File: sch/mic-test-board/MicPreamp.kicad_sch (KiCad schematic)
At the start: 30 parts, among them U7 ADA4940-2

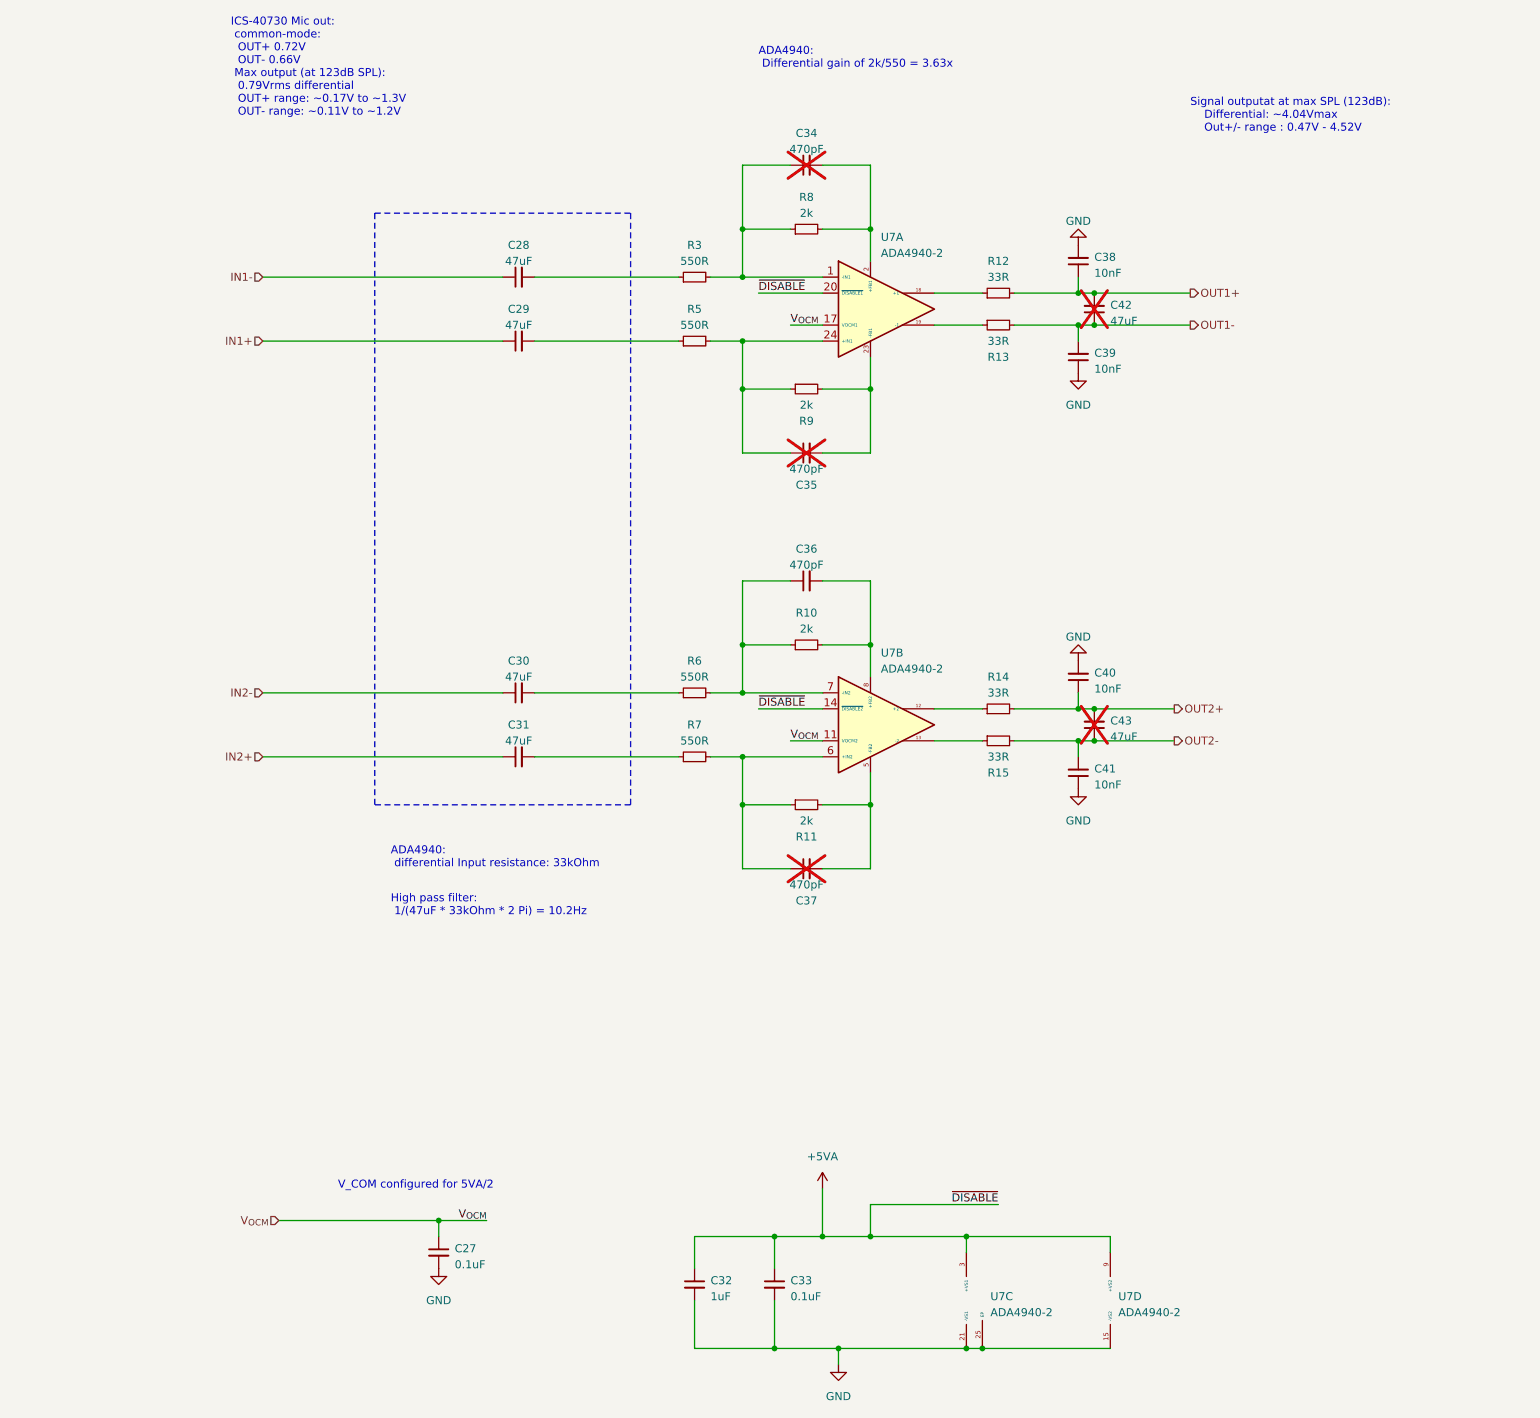
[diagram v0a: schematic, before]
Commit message: pcb: commit before large routing effort
 - schematic refactor to split preamps to each mic board
 - Mic board and main board are placed
 - no tracks laid
 - critical parts selected
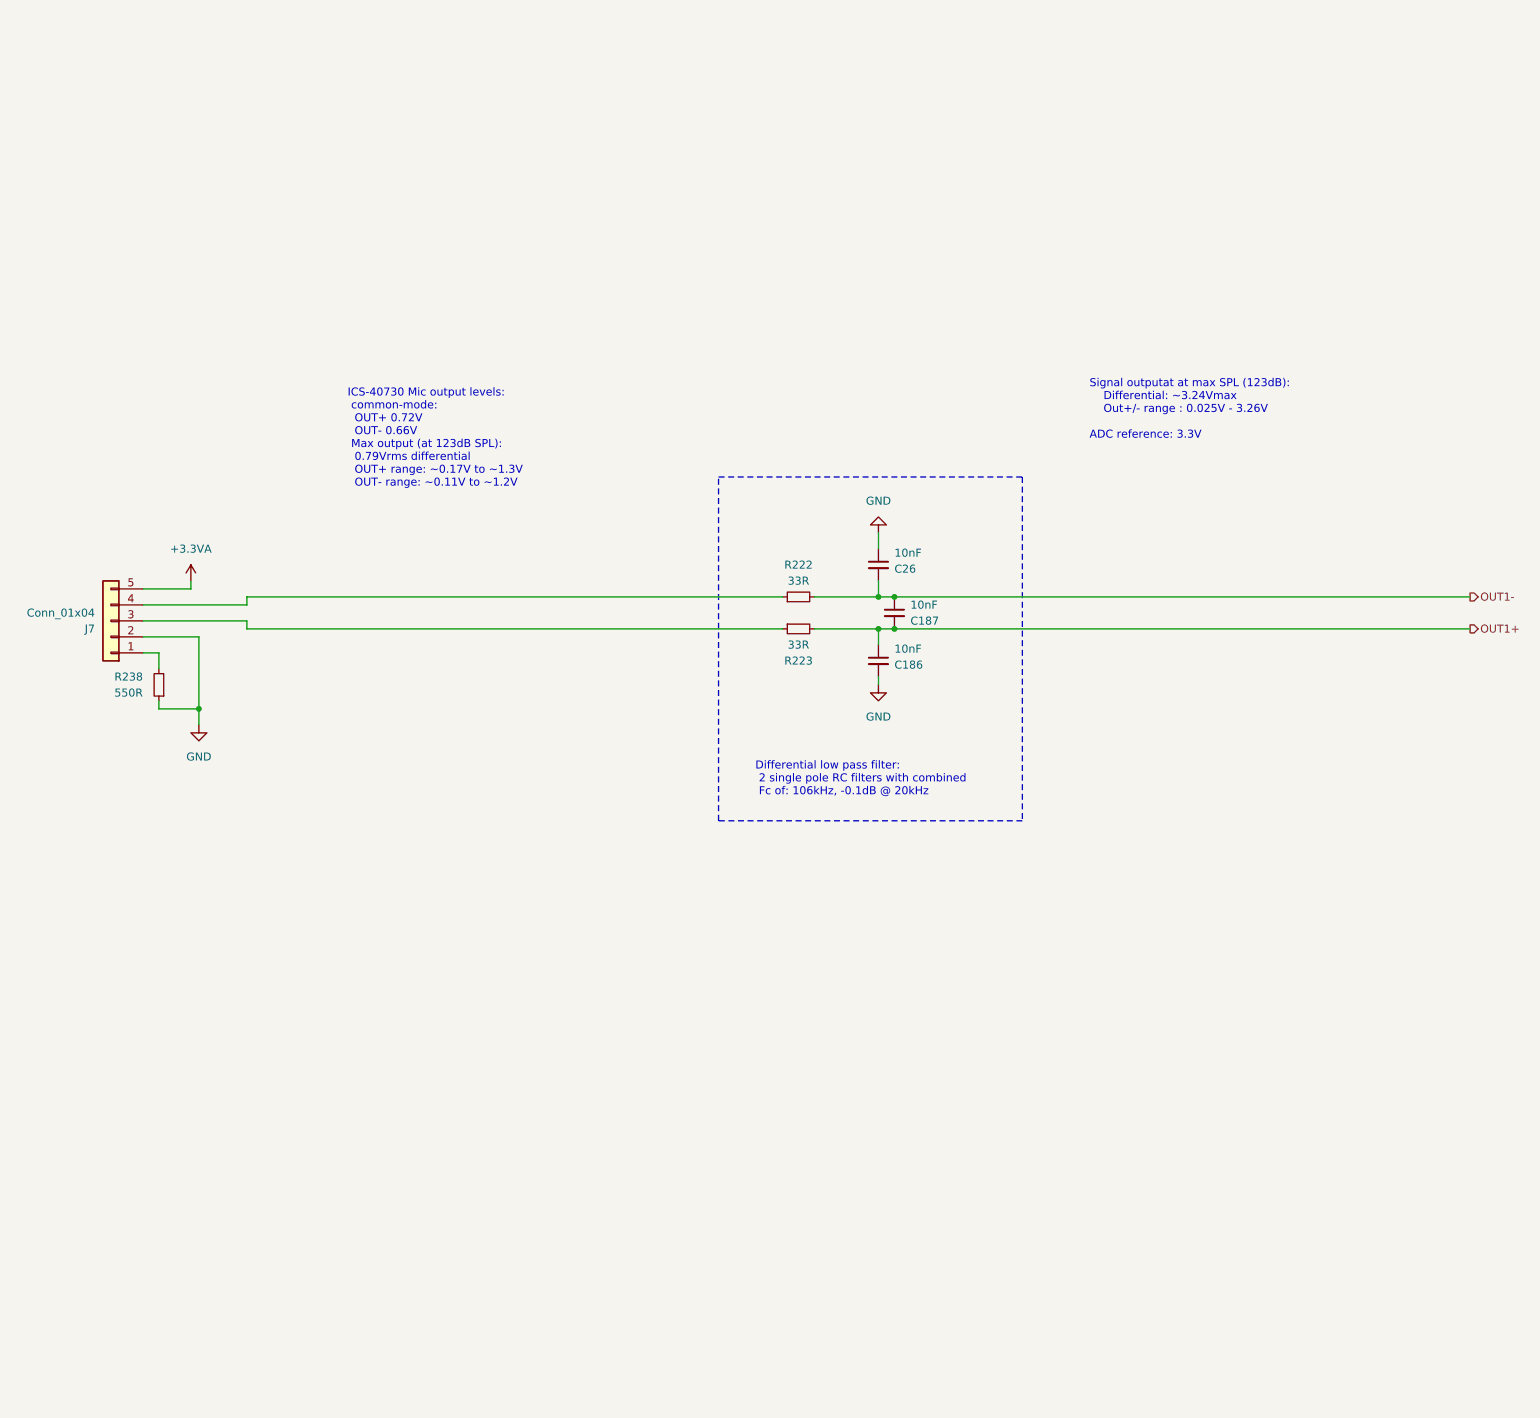
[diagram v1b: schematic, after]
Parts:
- removed C27, C33: 0.1uF, Capacitor_SMD:C_0603_1608Metric, symbol Device:C_Small
- removed C28, C29, C30, C31, C42, C43: 47uF, symbol Device:C_Small
- removed C32: 1uF, Capacitor_SMD:C_0603_1608Metric, symbol Device:C_Small
- removed C34, C35, C36, C37: 470pF, symbol Device:C_Small
- removed C38, C39, C40, C41: 10nF, symbol Device:C_Small
- removed R10, R11, R8, R9: 2k, symbol Device:R_Small
- removed R12, R13, R14, R15: 33R, symbol Device:R_Small
- removed R3, R5, R6, R7: 550R, symbol Device:R_Small
- removed U7: ADA4940-2, Package_CSP:LFCSP-24-1EP_4x4mm_P0.5mm_EP2.5x2.5mm, symbol mic-test-pcb:ADA4940-2
- added C186, C187, C26: 10nF, Capacitor_SMD:C_0603_1608Metric, symbol Device:C_Small
- added J7: Conn_01x04, Connector_Molex:Molex_PicoBlade_53047-0510_1x05_P1.25mm_Vertical, symbol Connector_Generic:Conn_01x05
- added R222, R223: 33R, Resistor_SMD:R_0603_1608Metric, symbol Device:R_Small
- added R238: 550R, Resistor_SMD:R_0603_1608Metric, symbol Device:R_Small
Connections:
- net GND: now also C186.2, C26.1, J7.2 (Pin_2), R238.1
- net OUT1+: now also C186.1, C187.2, R223.2
- net OUT1-: now also C187.1, C26.2, R222.2
- new net: J7.1 (Pin_1), R238.2
- new net: J7.3 (Pin_3), R223.1
- new net: J7.4 (Pin_4), R222.1
- new net +3.3VA: J7.5 (Pin_5)
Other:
- note added: "Differential low pass filter: 2 single pole RC filters with combined Fc of: 106kHz, -0.1dB @ 20kHz"
- note added: "ICS-40730 Mic output levels: common-mode: OUT+ 0.72V OUT- 0.66V Max output (at 123dB SPL): 0.79Vrms differential OUT+ range: ~0.17V to ~1.3V OUT- range: ~0.11V to ~1.2V"
- note added: "Signal outputat at max SPL (123dB): Differential: ~3.24Vmax Out+/- range : 0.025V - 3.26V ADC reference: 3.3V"
- note removed: "ADA4940: Differential gain of 2k/550 = 3.63x"
- note removed: "ADA4940: differential Input resistance: 33kOhm"
- note removed: "High pass filter: 1/(47uF * 33kOhm * 2 Pi) = 10.2Hz"
- note removed: "ICS-40730 Mic out: common-mode: OUT+ 0.72V OUT- 0.66V Max output (at 123dB SPL): 0.79Vrms differential OUT+ range: ~0.17V to ~1.3V OUT- range: ~0.11V to ~1.2V"
- note removed: "Signal outputat at max SPL (123dB): Differential: ~4.04Vmax Out+/- range : 0.47V - 4.52V"
- note removed: "V_COM configured for 5VA/2"
- company: (none) -> Josh Berry
- title: (none) -> Sound Compass POC
